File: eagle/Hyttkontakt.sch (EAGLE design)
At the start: 12 parts, among them J1 DT15-12PA

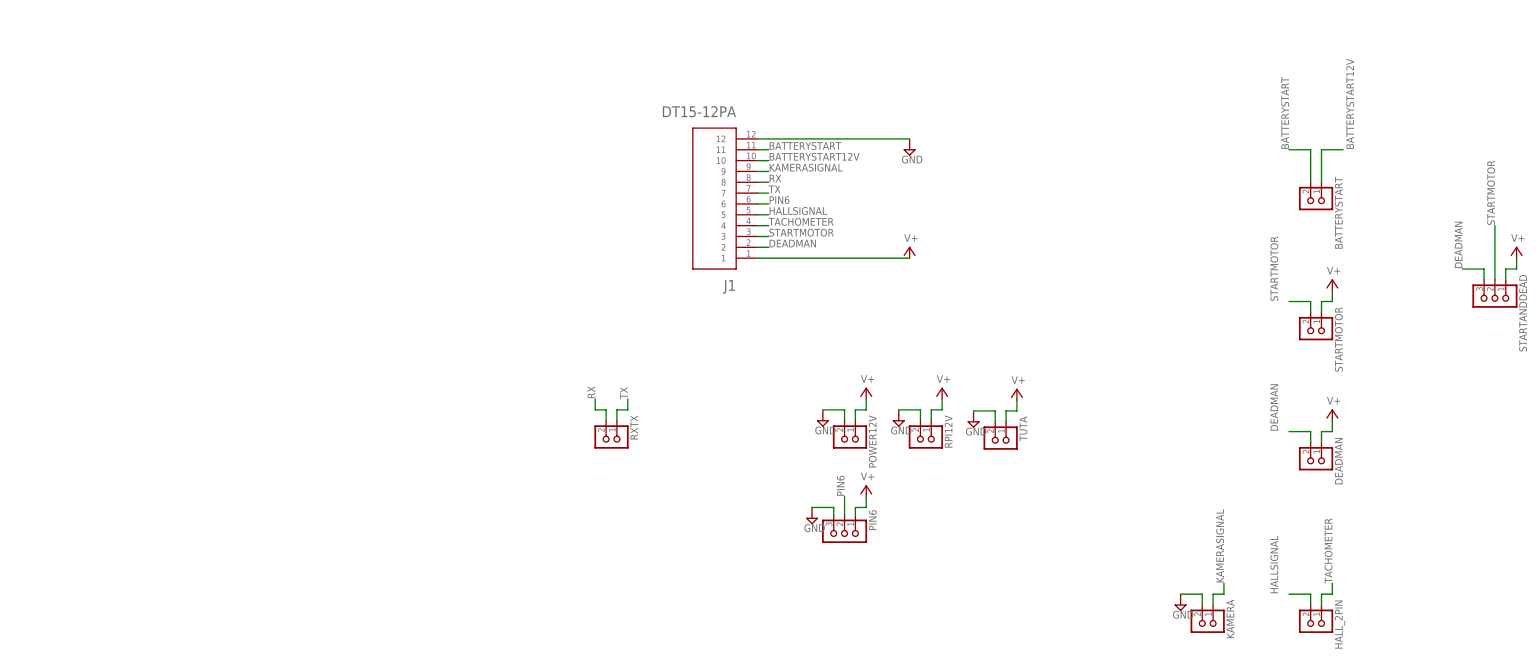
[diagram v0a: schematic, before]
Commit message: Updated layout (schematic)
Just updated the layout in the schematic. More clean now
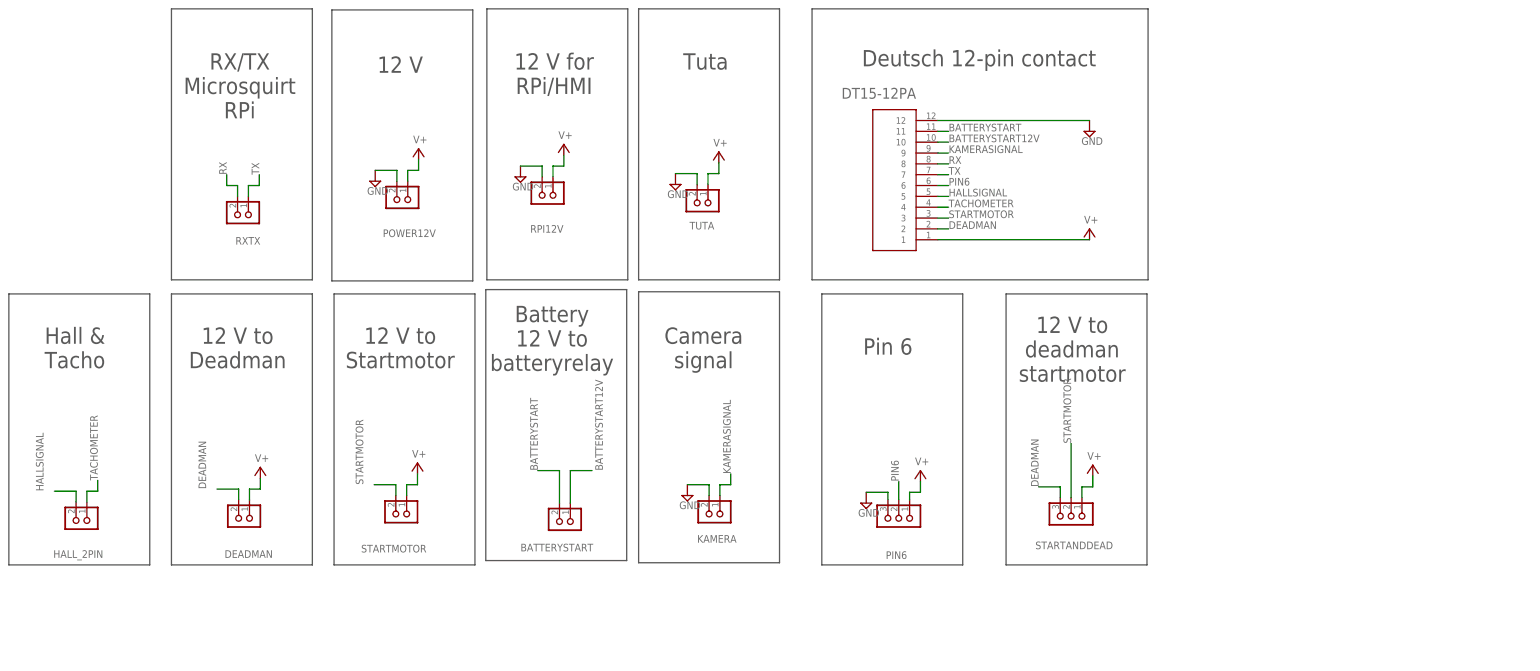
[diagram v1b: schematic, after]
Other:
- note added: "12 V"
- note added: "12 V for RPi/HMI"
- note added: "12 V to Deadman"
- note added: "12 V to Startmotor"
- note added: "12 V to deadman startmotor"
- note added: "Battery 12 V to batteryrelay"
- note added: "Camera signal"
- note added: "Deutsch 12-pin contact"
- note added: "Hall & Tacho"
- note added: "Pin 6"
- note added: "RX/TX Microsquirt RPi"
- note added: "Tuta"
- moved on the sheet: BATTERYSTART, DEADMAN, HALL_2PIN, KAMERA, PIN6, POWER12V, RPI12V, RXTX, STARTANDDEAD, STARTMOTOR, TUTA

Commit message: Bypass and easier connections
- HMI now goes on batterybypass connection
- Emergency button has its own connection in serie with HMI and Battery relay button
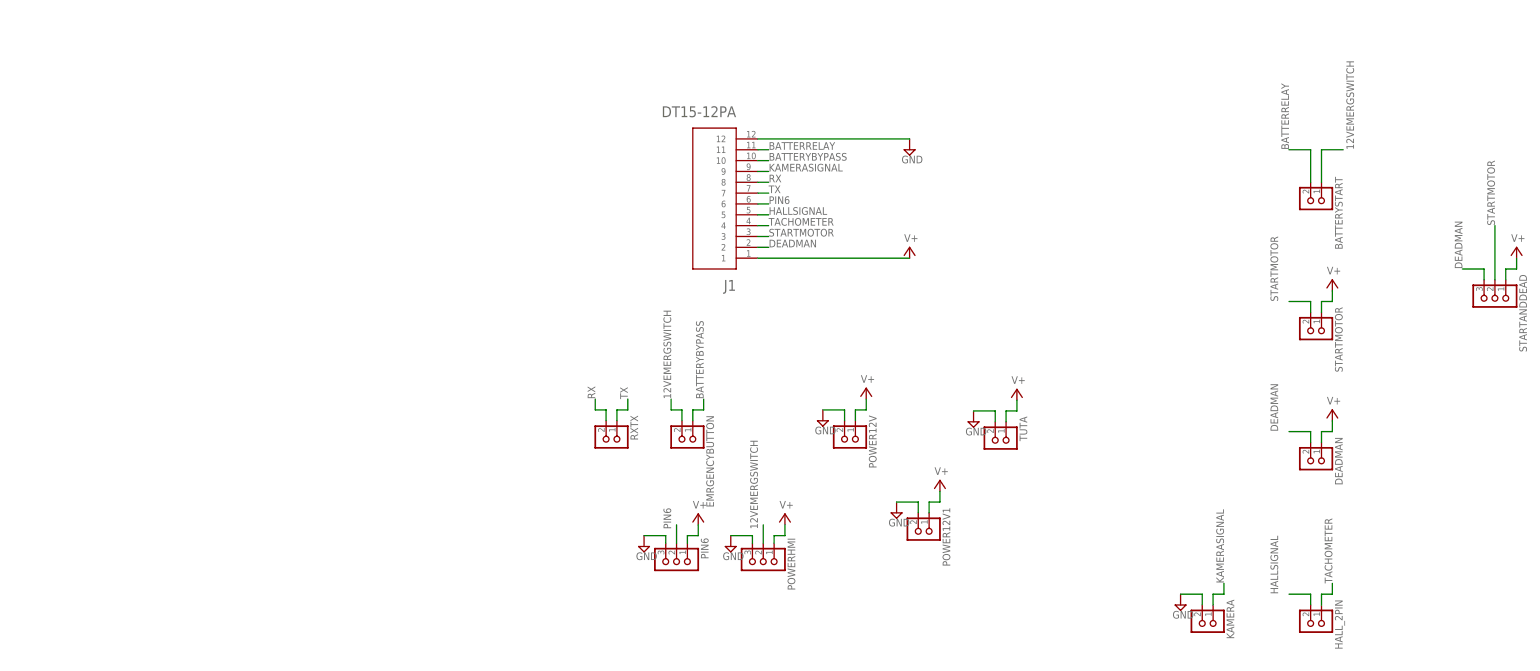
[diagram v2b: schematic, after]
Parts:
- removed RPI12V: EH_B2B-EH, CASE-JST:EH_B2B-EH
- added EMRGENCYBUTTON, POWER12V1: EH_B2B-EH, CASE-JST:EH_B2B-EH
- added POWERHMI: EH_B3B-EH, CASE-JST:EH_B3B-EH
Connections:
- net BATTERYSTART renamed BATTERRELAY
- removed net BATTERYSTART12V: BATTERYSTART.1, J1.10
- new net 12VEMERGSWITCH: BATTERYSTART.1, EMRGENCYBUTTON.2, POWERHMI.2
- new net BATTERYBYPASS: EMRGENCYBUTTON.1, J1.10
- net GND: now also POWER12V1.2, POWERHMI.3; no longer RPI12V.2
- net V+: now also POWER12V1.1, POWERHMI.1; no longer RPI12V.1
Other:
- note removed: "12 V"
- note removed: "12 V for RPi/HMI"
- note removed: "12 V to Deadman"
- note removed: "12 V to Startmotor"
- note removed: "12 V to deadman startmotor"
- note removed: "Battery 12 V to batteryrelay"
- note removed: "Camera signal"
- note removed: "Deutsch 12-pin contact"
- note removed: "Hall & Tacho"
- note removed: "Pin 6"
- note removed: "RX/TX Microsquirt RPi"
- note removed: "Tuta"
- moved on the sheet: BATTERYSTART, DEADMAN, HALL_2PIN, KAMERA, PIN6, POWER12V, RXTX, STARTANDDEAD, STARTMOTOR, TUTA
